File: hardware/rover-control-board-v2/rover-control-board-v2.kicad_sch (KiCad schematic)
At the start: 1 part

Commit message: Buses added
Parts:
- added J1, J2: M6 Terminal, symbol Connector:Screw_Terminal_01x01
- added J3: Contactor, symbol Connector_Generic:Conn_01x02
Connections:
- net GND: now reaches PCB1.20 (GND)
- net GND: now also PCB1.40 (GND), J2.1 (Pin_1)
- new net +BATT: J1.1 (Pin_1)
- new net contactor/COIL_H: J3.1 (Pin_1)
- new net contactor/COIL_L: J3.2 (Pin_2)
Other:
- sheet aux smart switch1 renamed aux1 smart switch
- added sheet aux2 smart switch (aux2_smart_switch.kicad_sch)
- added sheet contactor (contactor.kicad_sch)
- added sheet drive1 smart switch1 (drive1_smart_switch.kicad_sch)
- added sheet drive2 smart switch2 (drive2_smart_switch.kicad_sch)
- added sheet external smart switch (ext_smart_switch.kicad_sch)
- sheet aux1 smart switch: file aux_smart_switch.kicad_sch -> aux1_smart_switch.kicad_sch

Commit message: Started protection circuits
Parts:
- added 3V3, GND1: Testpoint, TestPoint:TestPoint_Pad_D2.0mm, symbol Connector:TestPoint
- added 3V3_IND1, VIN_IND1: LTST-C190KRKT, LED_SMD:LED_0603_1608Metric, symbol Device:LED
- added C10, C11: 22uF, Capacitor_SMD:C_0603_1608Metric, symbol Device:C
- added C12: 0.1uF, Capacitor_SMD:C_0402_1005Metric, symbol Device:C
- added C7: 4.7nF, symbol Device:C
- added C8: 10uF, Capacitor_SMD:C_0603_1608Metric, symbol Device:C
- added C9: Capacitor 100n 50V 0603, Capacitor_SMD:C_0603_1608Metric, symbol Device:C
- added D10, D11: FERD40, Package_TO_SOT_SMD:TO-263-2_TabPin1, symbol Device:D
- added D6, D8: B160-E3, Diode_SMD:D_SMA, symbol Diode:B160-E3
- added D9: 60V TVS, symbol Device:D_TVS
- added J10: CAN3, symbol Connector_Generic:Conn_01x02
- added J4: XT90_REG_OUT, symbol Connector_Generic:Conn_01x02
- added J5: XT90_REG_RET, symbol Connector_Generic:Conn_01x02
- added J6: OUT, symbol Connector:DE9_Socket_MountingHoles
- added J7: RET, symbol Connector:DE9_Socket_MountingHoles
- added J8: CAN1, symbol Connector_Generic:Conn_01x02
- added J9: CAN2, symbol Connector_Generic:Conn_01x02
- added L1: HPC4018NF-4R7M, Inductor_SMD:L_Taiyo-Yuden_MD-4040, symbol Device:L
- added R16, R18: 62R, symbol Device:R
- added R19, R21: Resistor 10k 0603, Resistor_SMD:R_0603_1608Metric, symbol Device:R
- added R20: 10k, Resistor_SMD:R_0402_1005Metric, symbol Device:R
- added VR1: AP63203WU-7, Package_TO_SOT_SMD:TSOT-23-6, symbol Regulator_Switching:AP63203WU
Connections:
- net +BATT: now also D10.1 (K), D11.1 (K), D6.2 (A), J4.1 (Pin_1); no longer J1.1 (Pin_1)
- net GND: now also C10.2, C11.2, C12.2, C7.2, C8.2, D9.1 (A1), GND1.1, J4.2 (Pin_2), J5.2 (Pin_2), R19.2, R21.2, VR1.4 (GND)
- net at PCB1.1 (VCC): now also D6.1 (K), D8.1 (K)
- net CAN_H: now reaches PCB1.7 (CAN_H)
- net CAN_H: now also J10.1 (Pin_1), J6.7, J8.1 (Pin_1), J9.1 (Pin_1)
- net CAN_L: now reaches PCB1.8 (CAN_L)
- net CAN_L: now also J10.2 (Pin_2), J6.2, J8.2 (Pin_2), J9.2 (Pin_2)
- new net: C7.1, R16.1, R18.1
- new net: J7.3, R18.2
- new net: R19.1, VIN_IND1.1 (K)
- new net: J7.2, R16.2
- new net: C9.1, L1.1, VR1.5 (SW)
- new net: D10.2 (A), D11.2 (A), D9.2 (A2), J1.1 (Pin_1)
- new net: C9.2, VR1.6 (BST)
- new net: 3V3_IND1.1 (K), R21.1
- new net: C12.1, R20.2, VR1.2 (EN)
- new net 3V3: 3V3.1, 3V3_IND1.2 (A), C10.1, C11.1, L1.2, VR1.1 (FB)
- new net JMP_PWR: D8.2 (A)
- new net VBUS: C8.1, J5.1 (Pin_1), R20.1, VIN_IND1.2 (A), VR1.3 (IN)
- no-connect marks 0 -> 8
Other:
- added sheet HV smart switch1 (HV_smart_switch.kicad_sch)
- note added: "2.5ms startup delay"
- note added: "Add FERD40H100SG-TR for reverse polarity protection (100V 40A)"
- note added: "Iout: 2A Max"
- note added: "VIN: 3.8 - 32V"
- note added: "When 6S battery is used, bypass external 24V regulator"
- moved on the sheet: J1, J2, J3, PCB1

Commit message: progress
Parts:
- added Q5: MCACD8D5N06YL-TP, symbol Transistor_FET:Q_Dual_NMOS_S1G1S2G2D2D2D1D1
- added U3: (no value), footprints:21-0137I_T633-2_MXM-L, symbol component_library:max6495
- added VBUS_TP: Testpoint, TestPoint:TestPoint_Pad_D2.0mm, symbol Connector:TestPoint
- D10: DigikeyPartNum (none) -> 497-16953-2-ND
- R19, R21: value Resistor 10k 0603 -> 10k
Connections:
- net GND: now also U3.4 (GND)
- net VBUS: now also Q5.1 (S), Q5.3 (S), U3.6 (OUTFB); no longer J5.1 (Pin_1)
- new net: J5.1 (Pin_1), Q5.5 (D), Q5.6 (D), Q5.7 (D), Q5.8 (D), U3.1 (IN), U3.2 (_SHDN), VBUS_TP.1
- new net: Q5.2 (G), Q5.4 (G), U3.5 (GATE)
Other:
- sheet comp smart switch ports: added 3V3, SCLK, SDATA; removed none
- moved on the sheet: 3V3, 3V3_IND1, C10, C11, C12, C7, C8, C9, GND1, J10, J5, J6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

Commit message: Further protections
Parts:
- removed D10, D11: FERD40, Package_TO_SOT_SMD:TO-263-2_TabPin1, symbol Device:D
- added C13: 50nF, symbol Device:C
- added C14: C_Polarized, symbol Device:C_Polarized
- added C15, C16, C17, C18: 1nF, symbol Device:C
- added Q6: MCACD8D5N06YL-TP, symbol Transistor_FET:Q_Dual_NMOS_S1G1S2G2D2D2D1D1
- added R26, R27, R28, R29: 100R, symbol Device:R
- added U4: LM74700, Package_TO_SOT_SMD:SOT-23-6, symbol Power_Management:LM74700
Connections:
- net +BATT: now also D9.2 (A2), J1.1 (Pin_1), C13.1, Q6.1 (S), Q6.3 (S), U4.3 (EN), U4.6 (ANODE)
- net GND: now also J6.SH (PAD), J7.SH (PAD), C14.2, C15.1, C16.2, C17.1, C18.1, U4.2 (GND)
- new net: C18.2, Q6.4 (G), R29.2
- new net: C14.1, Q6.5 (D), Q6.6 (D), Q6.7 (D), Q6.8 (D), U4.4 (CATHODE)
- new net: C17.2, Q6.2 (G), R28.1
- new net: R28.2, R29.1, U4.5 (GATE)
- new net: C13.2, U4.1 (VCAP)
- new net: C16.1, Q5.4 (G), R27.1
- new net: R26.1, R27.2, U3.5 (GATE)
- new net: C15.2, Q5.2 (G), R26.2
- no-connect marks 8 -> 15
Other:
- note added: "Could EN to SBB for control"
- note added: "Ideal diode, reverse polarity protection"
- note added: "REG bypass"
- note removed: "Add FERD40H100SG-TR for reverse polarity protection (100V 40A)"
- note removed: "When 6S battery is used, bypass external 24V regulator"
- moved on the sheet: 3V3, 3V3_IND1, C10, C11, C12, C7, C8, C9, GND1, J10, J4, J5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

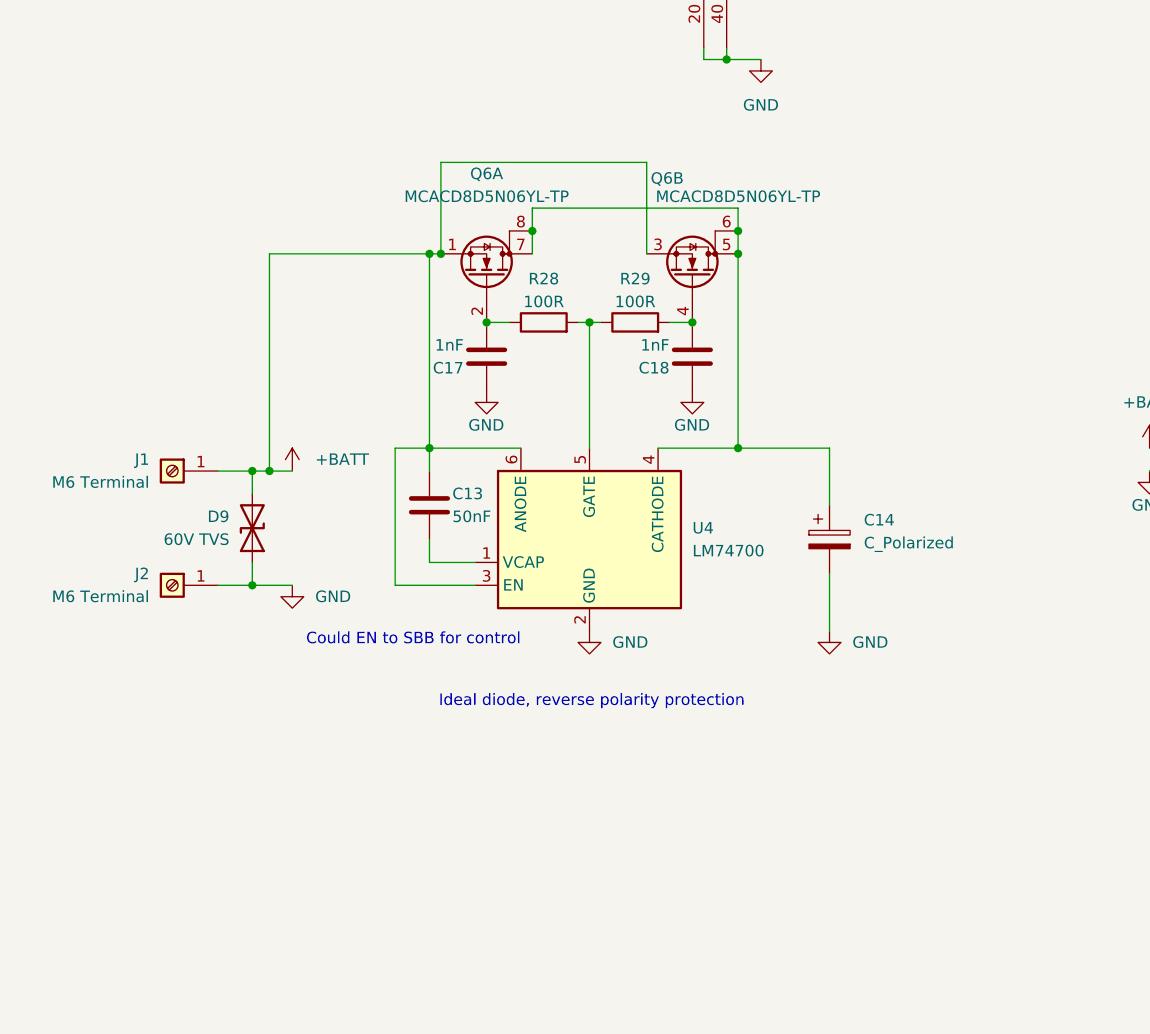
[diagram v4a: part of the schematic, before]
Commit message: still in the kitchen on voltage suppression
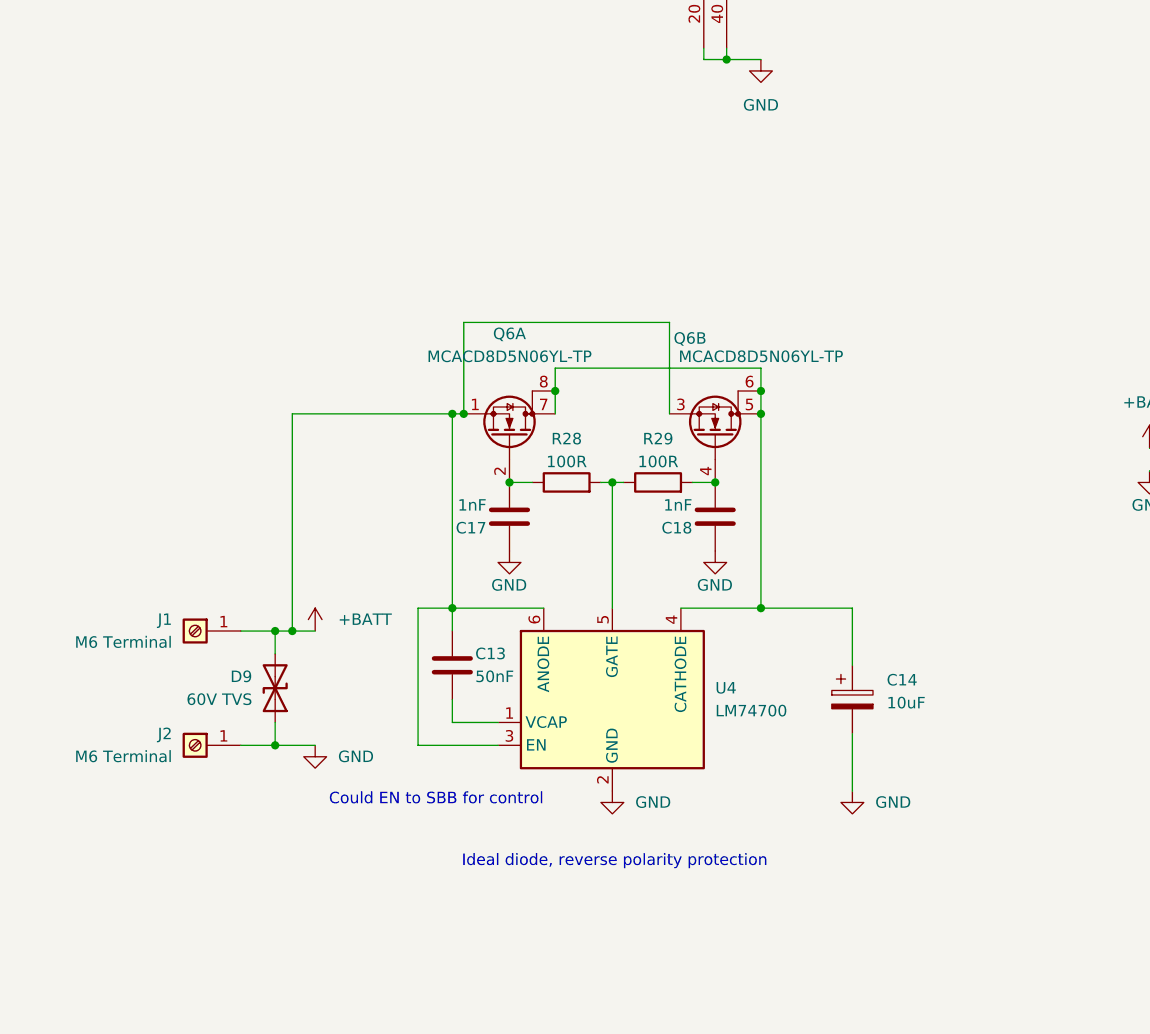
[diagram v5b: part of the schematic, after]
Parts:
- C14: value C_Polarized -> 10uF
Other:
- moved on the sheet: C13, C14, C17, C18, D9, J1, J2, Q6A, Q6B, R28, R29, U4

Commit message: Protections
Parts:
- removed J1, J2: M6 Terminal, symbol Connector:Screw_Terminal_01x01
- added BATT_IND, JMP_IND: LTST-C190KRKT, LED_SMD:LED_0603_1608Metric, symbol Device:LED
- added C19: 1uF, symbol Device:C
- added D10: SP0502BAHT, Package_TO_SOT_SMD:SOT-23, symbol Power_Protection:SP0502BAHT
- added J12: XT120, symbol Connector_Generic:Conn_01x02
- added R25, R30: 10k, Resistor_SMD:R_0603_1608Metric, symbol Device:R
- added R31: 500k, symbol Device:R
- added R32: 10k, symbol Device:R
- J3: footprint (none) -> Connector_JST:JST_XH_B2B-XH-A_1x02_P2.50mm_Vertical
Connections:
- net +BATT: now also C14.1, Q6.5 (D), Q6.6 (D), Q6.7 (D), Q6.8 (D), U4.4 (CATHODE), BATT_IND.2 (A), J12.1 (Pin_1), R31.2; no longer D6.2 (A)
- net GND: now also C19.2, J12.2 (Pin_2), R25.2, R30.2, R32.1
- net JMP_PWR: now also JMP_IND.2 (A)
- net VBUS: now also D6.2 (A)
- net at D6.1 (K), D8.1 (K), PCB1.1 (VCC): now also C19.1
- new net: BATT_IND.1 (K), R30.1
- new net: R31.1, R32.2
- new net: JMP_IND.1 (K), R25.1
- no-connect marks 15 -> 16
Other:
- note added: "ENSURE CONTACTOR COIL SUPPORTS 12-48V"
- note added: "JST-XH"

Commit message: Channels routed, temp bus pending
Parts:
- removed D10: SP0502BAHT, Package_TO_SOT_SMD:SOT-23, symbol Power_Protection:SP0502BAHT
- added C57, C58: 1nF, symbol Device:C
- added D10: ESD5Zxx, Diode_SMD:D_SOD-523, symbol Diode:ESD5Zxx
- added U17, U18: NMUX1308BQ, Package_DFN_QFN:DHVQFN-16-1EP_2.5x3.5mm_P0.5mm_EP1x2mm, symbol Analog_Switch:NMUX1308BQ
- added VBUS_TP1: Testpoint, TestPoint:TestPoint_Pad_D2.0mm, symbol Connector:TestPoint
- J10: value CAN3 -> CAN1; footprint (none) -> Connector_JST:JST_XH_B2B-XH-A_1x02_P2.50mm_Vertical
- J8: footprint (none) -> Connector_JST:JST_XH_B2B-XH-A_1x02_P2.50mm_Vertical
- J9: value CAN2 -> CAN1; footprint (none) -> Connector_JST:JST_XH_B2B-XH-A_1x02_P2.50mm_Vertical
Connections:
- net +BATT: now also VBUS_TP1.1; no longer C13.1, D9.2 (A2), J12.1 (Pin_1), Q6.1 (S), Q6.3 (S), R31.2, U4.3 (EN), U4.6 (ANODE)
- net 3V3: now also C57.2, C58.2, U17.16 (V_{CC}), U18.16 (V_{CC})
- net GND: now also C57.1, C58.1, D10.2 (A), U17.17 (EPAD), U17.6 (~{E}), U17.8 (GND), U18.17 (EPAD), U18.6 (~{E}), U18.8 (GND)
- net V_channel_mux: now reaches PCB1.10 (A2)
- net V_channel_mux: now also U18.3 (Z)
- net i_channel_mux: now reaches PCB1.11 (A3)
- net i_channel_mux: now also U17.3 (Z)
- net channel_mux_addr0: now reaches PCB1.12 (A4)
- net channel_mux_addr0: now also U17.11 (S0), U18.11 (S0)
- net channel_mux_addr1: now reaches PCB1.13 (A5)
- net channel_mux_addr1: now also U17.10 (S1), U18.10 (S1)
- net channel_mux_addr2: now reaches PCB1.14 (A6)
- net channel_mux_addr2: now also U17.9 (S2), U18.9 (S2)
- net comp_pre_en: now reaches PCB1.22 (IO13)
- net comp_ctrl: now reaches PCB1.23 (IO14)
- net drive_1_pre_en: now reaches PCB1.24 (IO21)
- net drive_1_ctrl: now reaches PCB1.25 (IO47)
- net drive_2_pre_en: now reaches PCB1.26 (IO48)
- net drive_2_ctrl: now reaches PCB1.27 (IO45)
- net aux_1_pre_en: now reaches PCB1.28 (IO37)
- net aux_1_ctrl: now reaches PCB1.29 (IO38)
- net aux_2_pre_en: now reaches PCB1.30 (IO39)
- net aux_2_ctrl: now reaches PCB1.31 (IO40)
- net ext_pre_en: now reaches PCB1.32 (IO41)
- net ext_ctrl: now reaches PCB1.33 (IO42)
- net HV_pre_en: now reaches PCB1.34 (IO16)
- net HV_ctrl: now reaches PCB1.35 (IO15)
- net VBATT_sense: now reaches PCB1.9 (A1)
- net VBATT_sense: now also R31.1, R32.2, D10.1 (K)
- new net: C13.1, D9.2 (A2), J12.1 (Pin_1), Q6.1 (S), Q6.3 (S), R31.2, U4.3 (EN), U4.6 (ANODE)
- new net HV_i_sense: U17.2 (Y6)
- new net HV_v_sense: U18.2 (Y6)
- new net aux1_v_sense: U18.12 (Y3)
- new net aux_1_i_sense: U17.12 (Y3)
- new net aux_2_i_sense: U17.1 (Y4)
- new net aux_2_v_sense: U18.1 (Y4)
- new net comp_i_sense: U17.13 (Y0)
- new net comp_v_sense: U18.13 (Y0)
- new net drive_1_i_sense: U17.14 (Y1)
- new net drive_1_v_sense: U18.14 (Y1)
- new net drive_2_v_sense: U18.15 (Y2)
- new net driver_2_i_sense: U17.15 (Y2)
- new net ext_i_sense: U17.5 (Y5)
- new net ext_v_sense: U18.5 (Y5)
- no-connect marks 16 -> 20
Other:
- sheet HV smart switch1 ports: added 3V3, SCLK, SDATA, TEMP_ALARM_, TEMP_INT_; removed none
- sheet aux1 smart switch ports: added 3V3, SCLK, SDATA, TEMP_ALARM_, TEMP_INT_; removed none
- sheet aux2 smart switch ports: added 3V3, SCLK, SDATA, TEMP_ALARM_, TEMP_INT_; removed none
- sheet comp smart switch ports: added TEMP_ALARM_, TEMP_INT_; removed none
- sheet drive1 smart switch1 ports: added 3V3, SCLK, SDATA, TEMP_ALARM_, TEMP_INT_; removed none
- sheet drive2 smart switch2 ports: added 3V3, SCLK, SDATA, TEMP_ALARM_, TEMP_INT_; removed none
- sheet external smart switch ports: added 3V3, SCLK, SDATA, TEMP_ALARM_, TEMP_INT_; removed none
- note added: "5v TVS"
- note added: "IS EN_ tied good?"
- moved on the sheet: D9, R32
